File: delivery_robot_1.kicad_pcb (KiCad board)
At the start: 4 copper layers, 100 x 100 mm, 105 parts, among them J1 SWD, J10 Port C/D breakout, J13 Pi 5 UART, J14 Pi 5 power, J15 Motor2 encoder, J16 MDD20A PWM2/DIR2/GND, J2 XT30PW-M, J4 BOOT0 jumper, J5 Power test points, J6 MDD20A PWM1/DIR1/GND, J7 Motor1 encoder, J8 Port A breakout, J9 Port B breakout, SW1 RESET, U1 STM32F091RCTx, U2 PTPSM63606RDLR, U3 TPS54202DDCR, U4 TPS7A8101DRBR, U5 PTPSM63606RDLR, U6 USBLC6-4SC6, U7 USBLC6-4SC6, Y3 8MHz

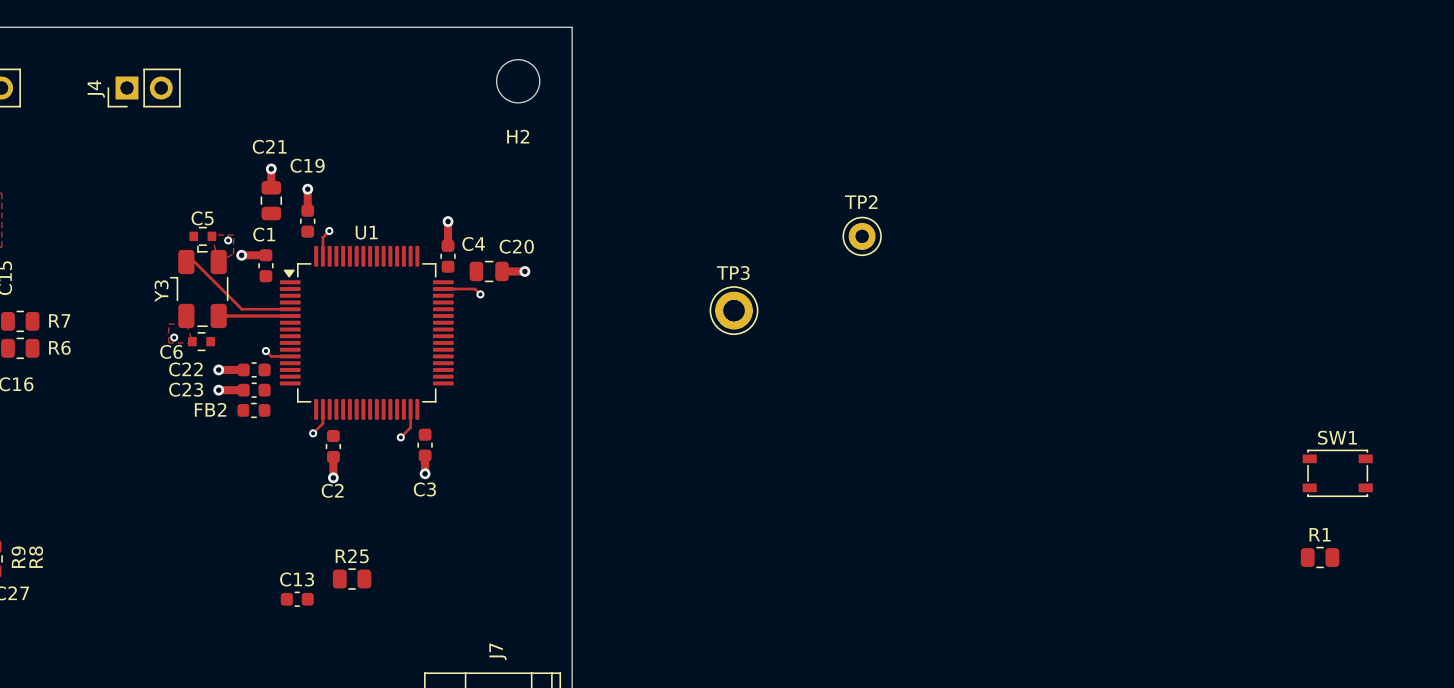
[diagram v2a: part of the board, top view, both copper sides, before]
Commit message: Place reset button and NRST pull-up; route NRST
- Place reset switch SW1 and NRST pull-up R1.
- Move C13, R25 and connector J4 (J4 is now unlocked).
- Route NRST, and add GND tracks and 3 GND vias.
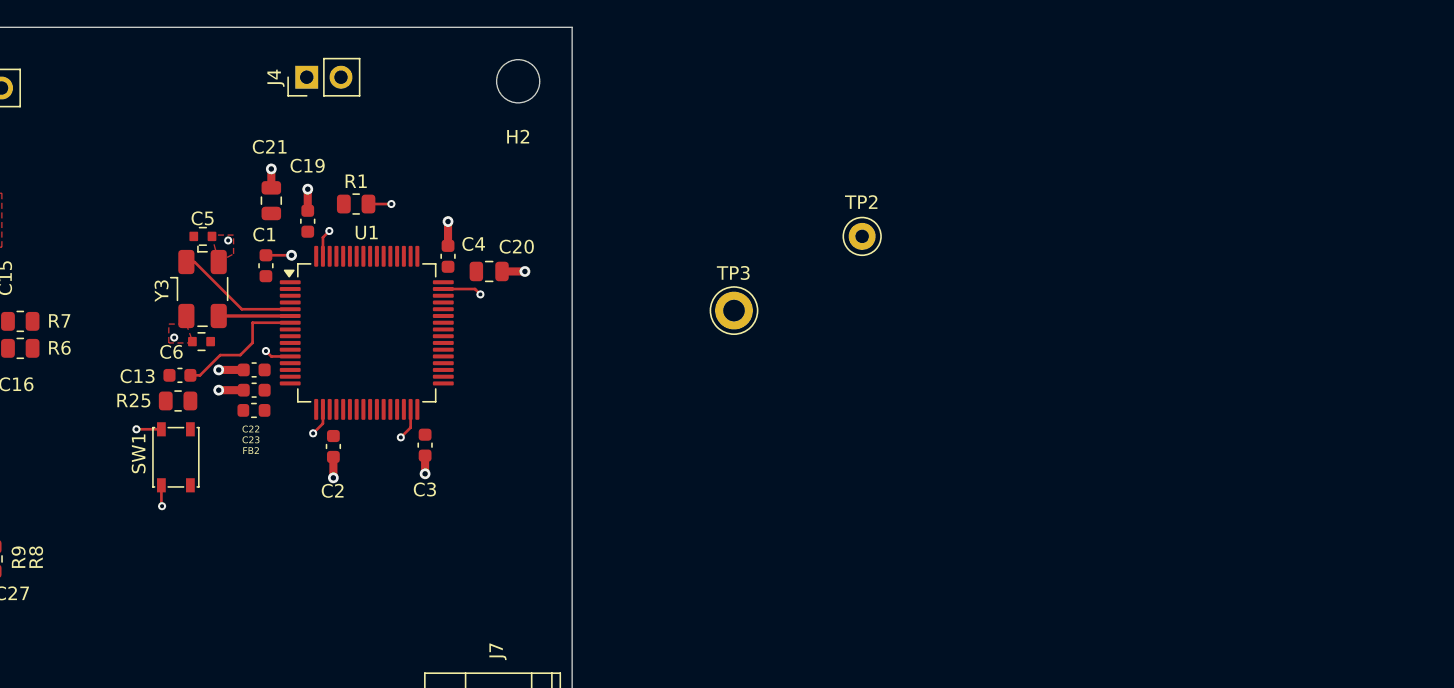
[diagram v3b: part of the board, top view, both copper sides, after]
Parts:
- moved SW1 86.1 mm to (155.6, 81.9), turned to -90 degrees
- moved R1 76.1 mm to (169.0, 63.1)
- moved C13 18.7 mm to (155.9, 75.8), turned to 180 degrees
- moved R25 18.5 mm to (155.8, 77.7)
- moved J4 13.3 mm to (165.3, 53.7)
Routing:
- net NRST: track 0.00 -> 9.89 mm
- net GND: track 26.3 -> 31.5 mm, vias 28 -> 31
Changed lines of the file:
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@@
 		(tags "inductor")
 		(property "Reference" "FB2"
-			(at 3.2125 0 0)
+			(at 0.2125 -3 0)
 			(layer "F.SilkS")
 			(effects
 				(font
-					(size 1 1)
-					(thickness 0.15)
+					(size 0.5 0.5)
+					(thickness 0.125)
 				)
 			)
@@
 	(footprint "Resistor_SMD:R_0805_2012Metric"
 		(layer "F.Cu")
-		(at 168.6875 90.9)
+		(at 155.7875 77.7)
 		(descr "Resistor SMD 0805 (2012 Metric), square (rectangular) end terminal, IPC-7351 nominal, (Body size source: IPC-SM-782 page 72, https://www.pcb-3d.com/wordpress/wp-content/uploads/ipc-sm-782a_amendment_1_and_2.pdf)")
 		(tags "resistor")
 		(property "Reference" "R25"
-			(at 0 -1.65 0)
+			(at -3.2875 0 0)
 			(layer "F.SilkS")
 			(effects
@@
 		(tags "capacitor")
 		(property "Reference" "C22"
-			(at 5.025 0 0)
+			(at 0.225 -4.4 0)
 			(layer "F.SilkS")
 			(effects
 				(font
-					(size 1 1)
-					(thickness 0.15)
+					(size 0.5 0.5)
+					(thickness 0.125)
 				)
 			)
@@
 	(footprint "Capacitor_SMD:C_0603_1608Metric"
 		(layer "F.Cu")
-		(at 164.625 92.4)
+		(at 155.925 75.8 180)
 		(descr "Capacitor SMD 0603 (1608 Metric), square (rectangular) end terminal, IPC-7351 nominal, (Body size source: IPC-SM-782 page 76, https://www.pcb-3d.com/wordpress/wp-content/uploads/ipc-sm-782a_amendment_1_and_2.pdf)")
 		(tags "capacitor")
 		(property "Reference" "C13"
-			(at 0 -1.43 0)
+			(at 3.125 -0.1 0)
 			(layer "F.SilkS")
 			(effects
@@
 		(duplicate_pad_numbers_are_jumpers no)
 		(fp_line
-			(start -0.14058 -0.51)
-			(end 0.14058 -0.51)
+			(start -0.14058 0.51)
+			(end 0.14058 0.51)
 			(stroke
 				(width 0.12)
@@
 		)
 		(fp_line
-			(start -0.14058 0.51)
-			(end 0.14058 0.51)
+			(start -0.14058 -0.51)
+			(end 0.14058 -0.51)
 			(stroke
 				(width 0.12)
@@
 		)
 		(pad "1" smd roundrect
-			(at -0.775 0)
+			(at -0.775 0 180)
 			(size 0.9 0.95)
 			(layers "F.Cu" "F.Mask" "F.Paste")
@@
 		)
 		(pad "2" smd roundrect
-			(at 0.775 0)
+			(at 0.775 0 180)
 			(size 0.9 0.95)
 			(layers "F.Cu" "F.Mask" "F.Paste")
@@
 	)
 	(footprint "Connector_PinHeader_2.54mm:PinHeader_1x02_P2.54mm_Vertical"
-		(locked yes)
 		(layer "F.Cu")
-		(at 152 54.5 90)
+		(at 165.325 53.7 90)
 		(descr "Through hole straight pin header, 1x02, 2.54mm pitch, single row")
 		(tags "Through hole pin header THT 1x02 2.54mm single row")
@@
 			(at 0 4.92 90)
 			(layer "F.Fab")
+			(hide yes)
 			(effects
 				(font
@@
 	(footprint "Button_Switch_SMD:SW_SPST_PTS810"
 		(layer "F.Cu")
-		(at 241.755 83.065)
+		(at 155.625 81.875 -90)
 		(descr "C&K Components, PTS 810 Series, Microminiature SMT Top Actuated, http://www.ckswitches.com/media/1476/pts810.pdf")
 		(tags "SPST Button Switch")
 		(property "Reference" "SW1"
-			(at 0 -2.6 0)
+			(at -0.275 2.725 90)
 			(layer "F.SilkS")
 			(effects
@@
 		)
 		(property "Value" "RESET"
-			(at 0 2.6 0)
+			(at 0 2.6 90)
 			(layer "F.Fab")
+			(hide yes)
 			(effects
 				(font
@@
 		)
 		(property "Datasheet" ""
-			(at 0 0 0)
+			(at 0 0 270)
 			(unlocked yes)
 			(layer "F.Fab")
@@
 		)
 		(property "Description" ""
-			(at 0 0 0)
+			(at 0 0 270)
 			(unlocked yes)
 			(layer "F.Fab")
@@
 		(duplicate_pad_numbers_are_jumpers no)
 		(fp_line
-			(start -2.2 -1.7)
-			(end -2.2 -1.58)
+			(start -2.2 1.7)
+			(end 2.2 1.7)
 			(stroke
 				(width 0.12)
@@
 		)
 		(fp_line
-			(start -2.2 -0.57)
-			(end -2.2 0.57)
+			(start 2.2 1.7)
+			(end 2.2 1.58)
 			(stroke
 				(width 0.12)
@@
 		)
 		(fp_line
-			(start -2.2 1.7)
-			(end 2.2 1.7)
+			(start 2.2 0.57)
+			(end 2.2 -0.57)
 			(stroke
 				(width 0.12)
@@
 		)
 		(fp_line
-			(start 2.2 -1.7)
-			(end -2.2 -1.7)
+			(start -2.2 -0.57)
+			(end -2.2 0.57)
 			(stroke
 				(width 0.12)
@@
 		)
 		(fp_line
-			(start 2.2 0.57)
-			(end 2.2 -0.57)
+			(start -2.2 -1.7)
+			(end -2.2 -1.58)
 			(stroke
 				(width 0.12)
@@
 		)
 		(fp_line
-			(start 2.2 1.7)
-			(end 2.2 1.58)
+			(start 2.2 -1.7)
+			(end -2.2 -1.7)
 			(stroke
 				(width 0.12)
@@
 		)
 		(fp_line
-			(start -2.85 -1.85)
-			(end 2.85 -1.85)
+			(start -2.85 1.85)
+			(end -2.85 -1.85)
 			(stroke
 				(width 0.05)
@@
 		)
 		(fp_line
-			(start -2.85 1.85)
-			(end -2.85 -1.85)
+			(start 2.85 1.85)
+			(end -2.85 1.85)
 			(stroke
 				(width 0.05)
@@
 		)
 		(fp_line
-			(start 2.85 -1.85)
-			(end 2.85 1.85)
+			(start -2.85 -1.85)
+			(end 2.85 -1.85)
 			(stroke
 				(width 0.05)
@@
 		)
 		(fp_line
-			(start 2.85 1.85)
-			(end -2.85 1.85)
+			(start 2.85 -1.85)
+			(end 2.85 1.85)
 			(stroke
 				(width 0.05)
@@
 		)
 		(fp_line
-			(start -2.1 -1.6)
-			(end -2.1 1.6)
+			(start -2.1 1.6)
+			(end 2.1 1.6)
 			(stroke
 				(width 0.1)
@@
 		)
 		(fp_line
-			(start -2.1 1.6)
-			(end 2.1 1.6)
+			(start 2.1 1.6)
+			(end 2.1 -1.6)
 			(stroke
 				(width 0.1)
@@
 		)
 		(fp_line
-			(start -0.4 -1.1)
-			(end 0.4 -1.1)
+			(start 0.4 1.1)
+			(end -0.4 1.1)
 			(stroke
 				(width 0.1)
@@
 		)
 		(fp_line
-			(start 0.4 1.1)
-			(end -0.4 1.1)
+			(start -0.4 -1.1)
+			(end 0.4 -1.1)
 			(stroke
 				(width 0.1)
@@
 		)
 		(fp_line
-			(start 2.1 -1.6)
-			(end -2.1 -1.6)
+			(start -2.1 -1.6)
+			(end -2.1 1.6)
 			(stroke
 				(width 0.1)
@@
 		)
 		(fp_line
-			(start 2.1 1.6)
-			(end 2.1 -1.6)
+			(start 2.1 -1.6)
+			(end -2.1 -1.6)
 			(stroke
 				(width 0.1)
@@
 		)
 		(fp_text user "${REFERENCE}"
-			(at 0 0 0)
+			(at 0 0 90)
 			(layer "F.Fab")
 			(effects
@@
 		)
 		(pad "1" smd rect
-			(at -2.075 -1.075)
+			(at -2.075 -1.075 270)
 			(size 1.05 0.65)
 			(layers "F.Cu" "F.Mask" "F.Paste")
@@
 		)
 		(pad "1" smd rect
-			(at 2.075 -1.075)
+			(at 2.075 -1.075 270)
 			(size 1.05 0.65)
 			(layers "F.Cu" "F.Mask" "F.Paste")
@@
 		)
 		(pad "2" smd rect
-			(at -2.075 1.075)
+			(at -2.075 1.075 270)
 			(size 1.05 0.65)
 			(layers "F.Cu" "F.Mask" "F.Paste")
@@
 		)
 		(pad "2" smd rect
-			(at 2.075 1.075)
+			(at 2.075 1.075 270)
 			(size 1.05 0.65)
 			(layers "F.Cu" "F.Mask" "F.Paste")
@@
 	(footprint "Resistor_SMD:R_0805_2012Metric"
 		(layer "F.Cu")
-		(at 240.445 89.305)
+		(at 168.9875 63.1)
 		(descr "Resistor SMD 0805 (2012 Metric), square (rectangular) end terminal, IPC-7351 nominal, (Body size source: IPC-SM-782 page 72, https://www.pcb-3d.com/wordpress/wp-content/uploads/ipc-sm-782a_amendment_1_and_2.pdf)")
 		(tags "resistor")
@@
 			(at 0 1.65 0)
 			(layer "F.Fab")
+			(hide yes)
 			(effects
 				(font
@@
 		(tags "capacitor")
 		(property "Reference" "C23"
-			(at 5.025 0 0)
+			(at 0.225 -3.7 0)
 			(layer "F.SilkS")
 			(effects
 				(font
-					(size 1 1)
-					(thickness 0.15)
+					(size 0.5 0.5)
+					(thickness 0.125)
 				)
 			)
@@
 	)
 	(segment
+		(start 154.55 79.8)
+		(end 152.7 79.8)
+		(width 0.2)
+		(layer "F.Cu")
+		(net "GND")
+	)
+	(segment
 		(start 173.025 78.325)
 		(end 173.025 79.675)
@@
 	)
 	(segment
+		(start 154.55 85.45)
+		(end 154.6 85.5)
+		(width 0.2)
+		(layer "F.Cu")
+		(net "GND")
+	)
+	(segment
+		(start 169.9 63.1)
+		(end 171.6 63.1)
+		(width 0.2)
+		(layer "F.Cu")
+		(net "GND")
+	)
+	(segment
 		(start 179.8 68.1)
 		(end 181.5 68.1)
@@
 	)
 	(segment
-		(start 162.3 66.9)
-		(end 160.5 66.9)
-		(width 0.6)
+		(start 154.55 83.95)
+		(end 154.55 85.45)
+		(width 0.2)
 		(layer "F.Cu")
 		(net "GND")
@@
 	)
 	(segment
+		(start 162.3 66.9)
+		(end 164.2 66.9)
+		(width 0.2)
+		(layer "F.Cu")
+		(net "GND")
+	)
+	(segment
 		(start 173.025 79.675)
 		(end 172.3 80.4)
@@
 	)
 	(via
+		(at 171.6 63.1)
+		(size 0.6)
+		(drill 0.3)
+		(layers "F.Cu" "B.Cu")
+		(net "GND")
+	)
+	(via
+		(at 154.6 85.5)
+		(size 0.6)
+		(drill 0.3)
+		(layers "F.Cu" "B.Cu")
+		(net "GND")
+	)
+	(via
 		(at 138.3 70.4)
 		(size 0.6)
@@
 	)
 	(via
-		(at 160.5 66.9)
+		(at 164.2 66.9)
 		(size 0.8)
 		(drill 0.4)
@@
 	)
 	(via
+		(at 152.7 79.8)
+		(size 0.6)
+		(drill 0.3)
+		(layers "F.Cu" "B.Cu")
+		(net "GND")
+	)
+	(via
 		(at 162.7 60.5)
 		(size 0.8)
@@
 	)
 	(segment
+		(start 158.91005 74.3)
+		(end 157.41005 75.8)
+		(width 0.2)
+		(layer "F.Cu")
+		(net "NRST")
+	)
+	(segment
+		(start 161.31005 71.9)
+		(end 161.31005 73.38995)
+		(width 0.2)
+		(layer "F.Cu")
+		(net "NRST")
+	)
+	(segment
+		(start 157.41005 75.8)
+		(end 156.7 75.8)
+		(width 0.2)
+		(layer "F.Cu")
+		(net "NRST")
+	)
+	(segment
+		(start 161.31005 73.38995)
+		(end 160.4 74.3)
+		(width 0.2)
+		(layer "F.Cu")
+		(net "NRST")
+	)
+	(segment
+		(start 160.4 74.3)
+		(end 158.91005 74.3)
+		(width 0.2)
+		(layer "F.Cu")
+		(net "NRST")
+	)
+	(segment
+		(start 164.1 71.9)
+		(end 161.31005 71.9)
+		(width 0.2)
+		(layer "F.Cu")
+		(net "NRST")
+	)
+	(segment
